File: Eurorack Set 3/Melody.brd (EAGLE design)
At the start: 59.6 x 106.5 mm, 137 parts, among them IC1 LD1117AS33TR, IC3 TL074D, IC4 MCP6004, Q1 MMBT3904, Q2 MMBT3904, Q3 MMBT3904, Q4 MMBT3904, Q5 MMBT3904, Q6 MMBT3904, Q7 MMBT3904, Q8 MMBT3904, U1 MKL02Z32VFK4, U2 LM4040DIM3-5.0, U3 74HC595BQ, U4 74HC595BQ, U5 74HC595BQ, U6 24LC00T-I/OT

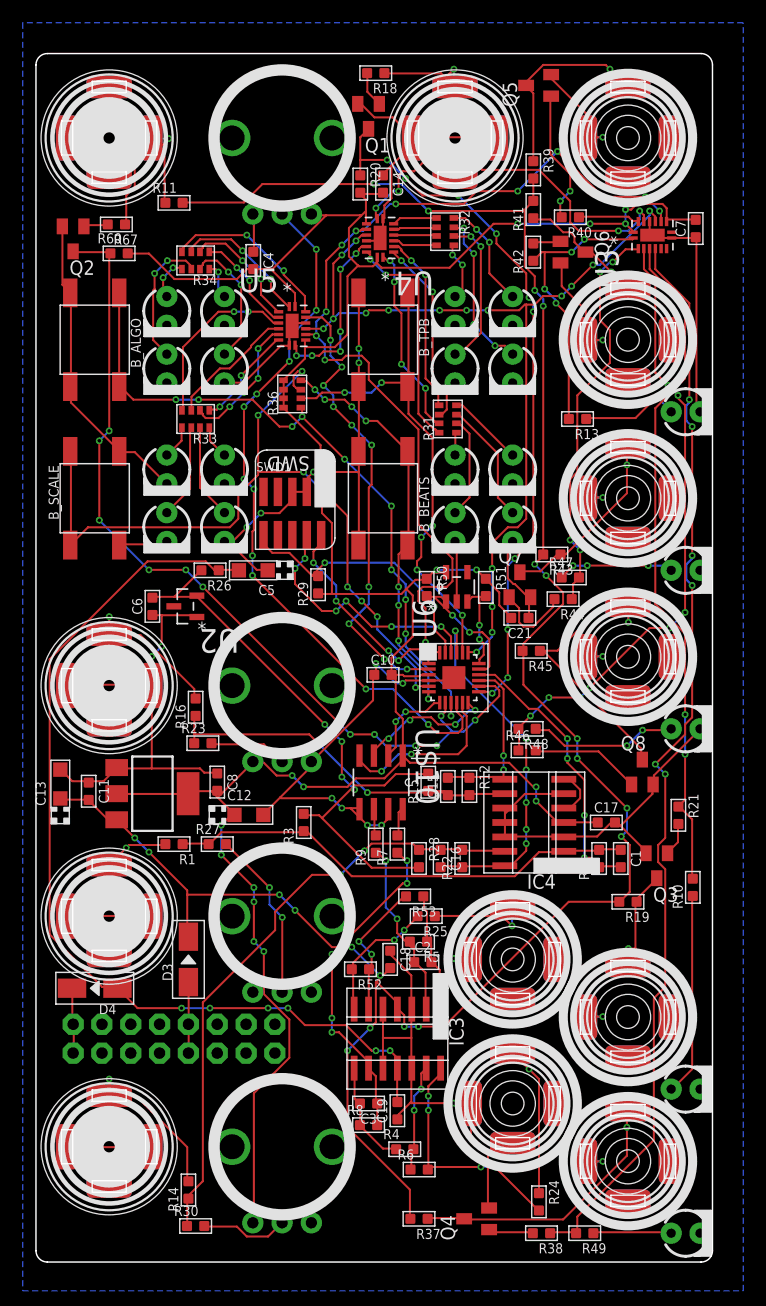
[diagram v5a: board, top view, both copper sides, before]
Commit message: Added Simple Switch Module - Added DESC attribute for some input elements
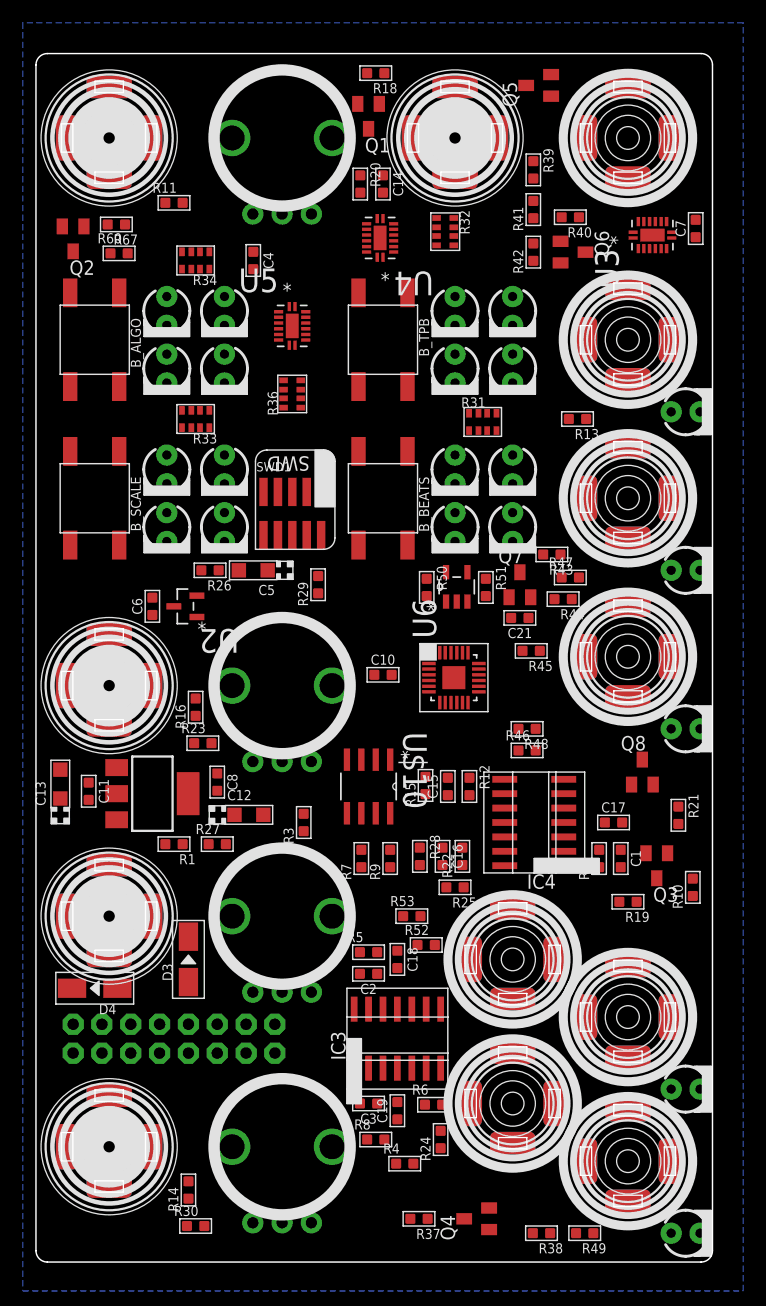
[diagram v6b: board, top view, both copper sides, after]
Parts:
- ACCENT: value ACCENT -> PJ-341
- BEAT: value Beat -> PJ-341
- C1, C15, C16, C2, C3: value 3.3n -> 3.3nF
- CLOCK: value Clock In -> PJ-341
- CLOCKOUT_JACK: value Clock Out -> PJ-341
- GATE: value GATE -> PJ-341
- IN1: value In 1 -> PJ-341
- IN2: value In 2 -> PJ-341
- INTENSITY: value INTENSITY -> PJ-341
- LOOP: value Loop -> PJ-341
- NOTE: value NOTE -> PJ-341
- RESET: value Reset -> PJ-341
- TICK: value Tick -> PJ-341
- VELOCITY: value VELOCITY -> PJ-341
- moved R24 10.3 mm to (36.8, 10.8), turned to 90 degrees
- moved R52 6.18 mm to (35.6, 27.9), turned to 0 degrees
- moved R6 5.85 mm to (36.2, 13.9)
- moved C2 4.89 mm to (30.5, 25.4), turned to 180 degrees
- moved R5 4.50 mm to (30.5, 27.3), turned to 0 degrees
- moved R25 3.59 mm to (38.1, 33.0)
- moved R7 3.42 mm to (29.8, 35.6)
- moved R31 3.09 mm to (40.5, 74.0), turned to 0 degrees
- moved R9 1.80 mm to (32.4, 35.6)
- moved R53 1.76 mm to (34.3, 30.5), turned to 0 degrees
- moved R8 1.42 mm to (31.1, 10.8)
- moved R4 1.27 mm to (33.7, 8.67)
- moved U$10 1.16 mm to (30.5, 41.9)
- moved C18 0.64 mm to (33.0, 26.7)
- moved C17 0.63 mm to (52.1, 38.7)
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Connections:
- removed net N$11: R7.2, U$10.8
- removed net N$12: R9.2, U$10.6
- new net N$5: R9.2, U$10.8
- new net N$7: R7.2, U$10.6
- net N$10: now also IC3.2; no longer IC3.9
- net N$14: now also IC3.7; no longer IC3.14
- net N$17: now also IC3.9; no longer IC3.6
- net N$18: now also IC3.1; no longer IC3.8
- net N$2: now also IC3.6; no longer IC3.13
- net N$24: now also IC3.14; no longer IC3.1
- net N$9: now also IC3.13; no longer IC3.2
- net N$94: now also IC3.8; no longer IC3.7
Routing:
- net GND: track 361.2 -> 0.00 mm, vias 27 -> 0
- net 3.3V: track 246.8 -> 0.00 mm, vias 16 -> 0
- net 12V: track 197.4 -> 0.00 mm, vias 20 -> 0
- net OUT_GATE: track 96.6 -> 0.00 mm, vias 6 -> 0
- net CLOCK: track 84.7 -> 0.00 mm, vias 12 -> 0
- net -12V: track 83.9 -> 0.00 mm, vias 6 -> 0
- net LATCH: track 78.6 -> 0.00 mm, vias 17 -> 0
- net CLOCK_IN: track 78.2 -> 0.00 mm, vias 13 -> 0
- net BUTTON_SCALE: track 70.3 -> 0.00 mm, vias 8 -> 0
- net RESET_PATTERN: track 63.7 -> 0.00 mm, vias 10 -> 0
- net KNOB_TEMPO: track 63.1 -> 0.00 mm, vias 11 -> 0
- net BUTTON_ALGO: track 60.0 -> 0.00 mm, vias 10 -> 0
- net OUT_ACCENT: track 59.8 -> 0.00 mm, vias 2 -> 0
- net OUT_LOOP: track 54.6 -> 0.00 mm, vias 8 -> 0
- net N$34: track 54.0 -> 0.00 mm, vias 2 -> 0
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
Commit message: added router settings, Melody polishing
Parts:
- added U$19: SMALLROCKET, zephod-components:SMALLROCKET
- added U$4, U$7, U$8: FIDUCIAL, adafruit:FIDUCIAL_1MM
- C18, C19: value 100nF -> 100nF 16V+
- moved C7 14.8 mm to (46.3, 84.1)
- moved R42 14.0 mm to (59.0, 88.2)
- moved C18 13.6 mm to (33.0, 13.1), turned to 90 degrees
- moved C19 13.3 mm to (33.2, 26.7), turned to 270 degrees
- moved C14 10.6 mm to (27.0, 85.5), turned to 90 degrees
- moved U3 9.28 mm to (46.2, 89.8), turned to 180 degrees
- moved Q6 6.91 mm to (55.2, 90.5), turned to 90 degrees
- moved R41 6.41 mm to (51.0, 90.5), turned to 180 degrees
- moved R48 5.35 mm to (49.8, 46.2)
- moved R46 5.33 mm to (49.8, 44.5)
- moved R40 5.21 mm to (44.8, 96.0), turned to 90 degrees
- moved R21 4.15 mm to (58.2, 35.2), turned to 180 degrees
- moved Q3 3.78 mm to (56.4, 31.2)
- moved R22 3.51 mm to (42.2, 36.0)
- moved C1 3.32 mm to (56.0, 36.0)
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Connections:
- net GND: now also ACCENT.RING@3, BEAT.RING@3, CLOCK.RING@3, CLOCKOUT_JACK.RING@3, GATE.RING@3, IN1.RING@3, IN1.SWITCH@3, IN2.RING@3, IN2.SWITCH@3, INTENSITY.RING@3, INTENSITY.SWITCH@3, LOOP.RING@3, NOTE.RING@3, RESET.RING@3, RESET.SWITCH@3, TICK.RING@3, VELOCITY.RING@3; no longer ACCENT.RING@1, ACCENT.RING@2, BEAT.RING@1, BEAT.RING@2, CLOCK.RING@1, CLOCK.RING@2, CLOCKOUT_JACK.RING@1, CLOCKOUT_JACK.RING@2, GATE.RING@1, GATE.RING@2, IN1.RING@1, IN1.RING@2, IN1.SWITCH@1, IN1.SWITCH@2, IN2.RING@1, IN2.RING@2, IN2.SWITCH@1, IN2.SWITCH@2, INTENSITY.RING@1, INTENSITY.RING@2, INTENSITY.SWITCH@1, INTENSITY.SWITCH@2, LOOP.RING@1, LOOP.RING@2, NOTE.RING@1, NOTE.RING@2, RESET.RING@1, RESET.RING@2, RESET.SWITCH@1, RESET.SWITCH@2, TICK.RING@1, TICK.RING@2, VELOCITY.RING@1, VELOCITY.RING@2
- net N$16: now also RESET.TIP@3; no longer RESET.TIP@1, RESET.TIP@2
- net N$20: now also VELOCITY.TIP@3; no longer VELOCITY.TIP@1, VELOCITY.TIP@2
- net N$21: now also NOTE.TIP@3; no longer NOTE.TIP@1, NOTE.TIP@2
- net N$29: now also ACCENT.TIP@3; no longer ACCENT.TIP@1, ACCENT.TIP@2
- net N$3: now also IN1.TIP@3; no longer IN1.TIP@1, IN1.TIP@2
- net N$33: now also INTENSITY.TIP@3; no longer INTENSITY.TIP@1, INTENSITY.TIP@2
- net N$43: now also CLOCK.TIP@3; no longer CLOCK.TIP@1, CLOCK.TIP@2
- net N$58: now also GATE.TIP@3; no longer GATE.TIP@1, GATE.TIP@2
- net N$6: now also IN2.TIP@3; no longer IN2.TIP@1, IN2.TIP@2
- net N$61: now also CLOCKOUT_JACK.TIP@3; no longer CLOCKOUT_JACK.TIP@1, CLOCKOUT_JACK.TIP@2
- net N$65: now also TICK.TIP@3; no longer TICK.TIP@1, TICK.TIP@2
- net N$69: now also BEAT.TIP@3; no longer BEAT.TIP@1, BEAT.TIP@2
- net N$72: now also LOOP.TIP@3; no longer LOOP.TIP@1, LOOP.TIP@2
- net N$96: now also CLOCK.SWITCH@3; no longer CLOCK.SWITCH@1, CLOCK.SWITCH@2
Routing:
- net GND: track 0.00 -> 330.8 mm, vias 0 -> 46
- net 3.3V: track 0.00 -> 247.8 mm, vias 0 -> 27
- net 12V: track 0.00 -> 195.6 mm, vias 0 -> 26
- net OUT_GATE: track 0.00 -> 101.2 mm, vias 0 -> 6
- net KNOB_TEMPO: track 0.00 -> 100.7 mm, vias 0 -> 6
- net -12V: track 0.00 -> 87.3 mm, vias 0 -> 4
- net CLOCK_IN: track 0.00 -> 79.9 mm, vias 0 -> 7
- net LATCH: track 0.00 -> 72.0 mm, vias 0 -> 6
- net CLOCK: track 0.00 -> 70.5 mm, vias 0 -> 12
- net BUTTON_SCALE: track 0.00 -> 67.7 mm, vias 0 -> 8
- net OUT_ACCENT: track 0.00 -> 66.5 mm, vias 0 -> 2
- net RESET_PATTERN: track 0.00 -> 63.9 mm, vias 0 -> 10
- net BUTTON_ALGO: track 0.00 -> 63.9 mm, vias 0 -> 4
- net N$34: track 0.00 -> 58.5 mm, vias 0 -> 6
- net REF_-5V: track 0.00 -> 53.3 mm, vias 0 -> 8
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
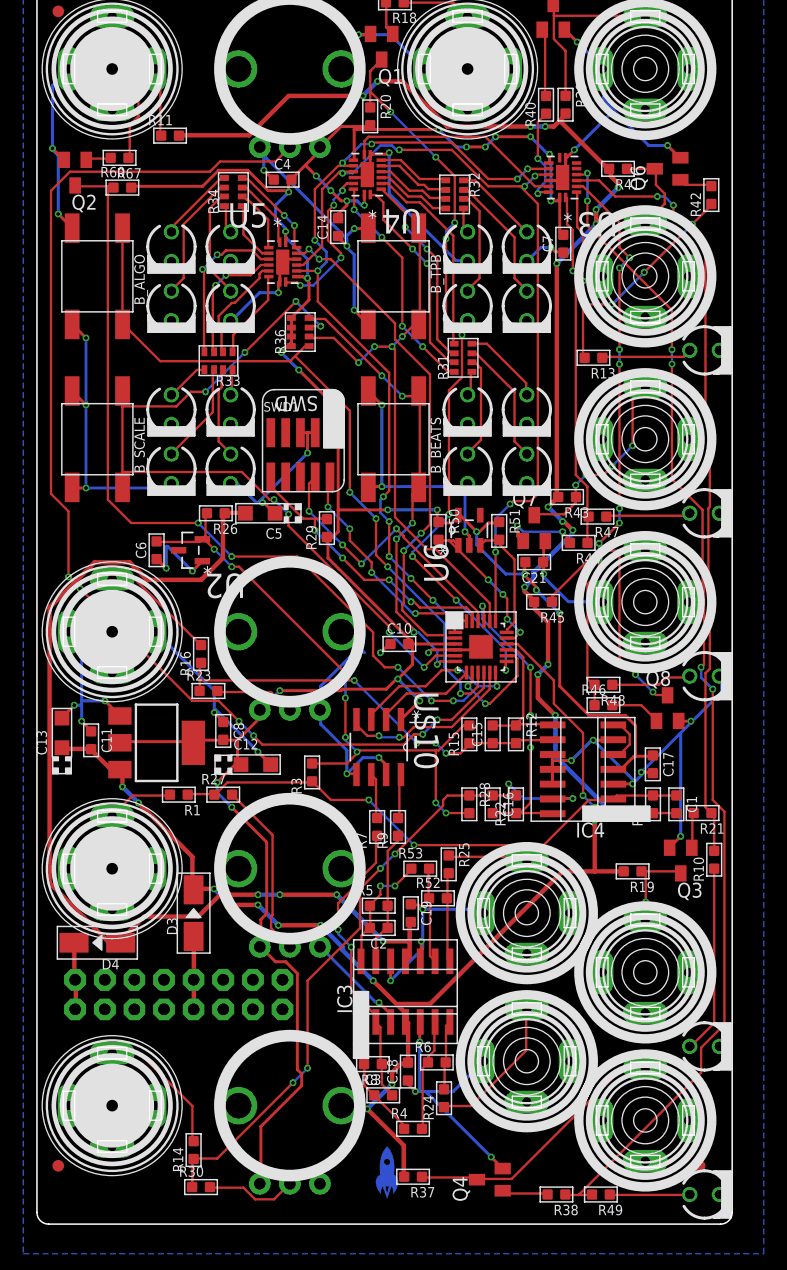
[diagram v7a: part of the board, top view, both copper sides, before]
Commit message: Clearance updates - removed double clocktrace
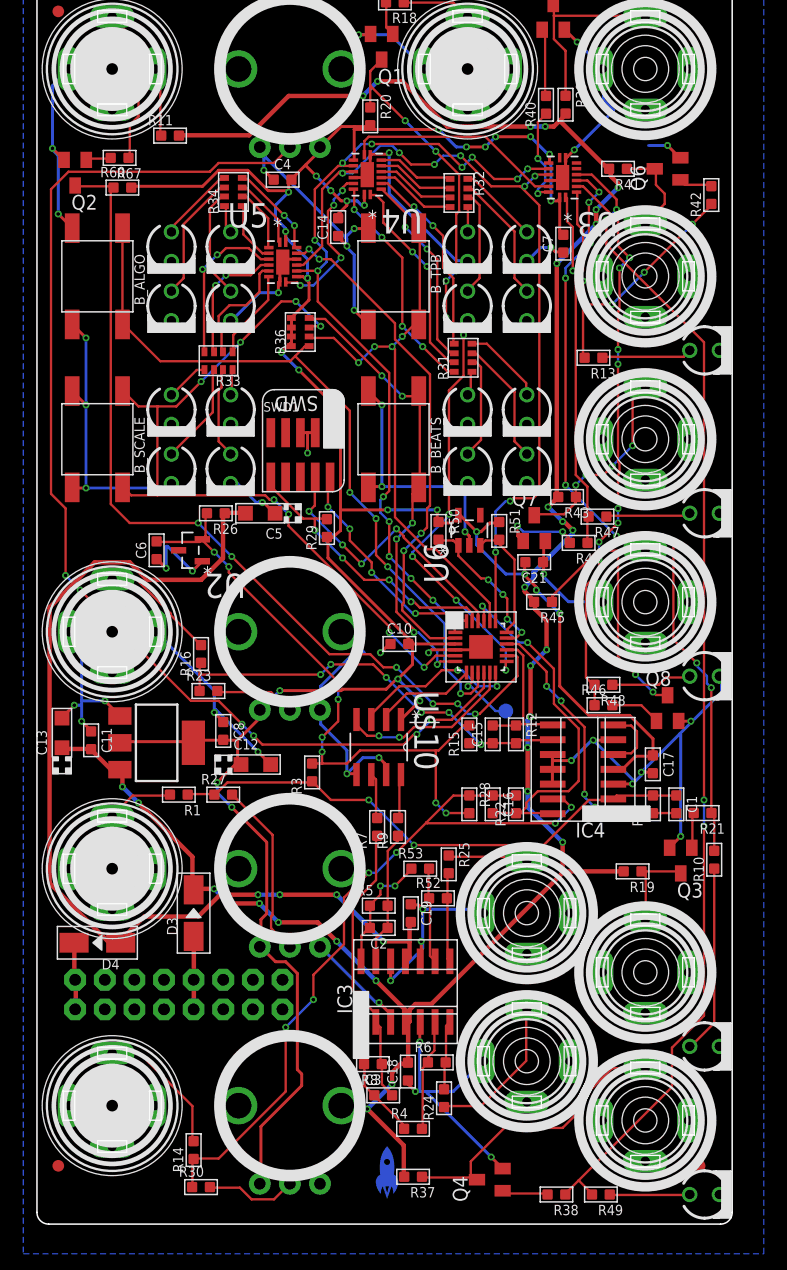
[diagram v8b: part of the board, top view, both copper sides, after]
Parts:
- added TP1: TPB1,27, testpad:B1,27
- moved R32 0.40 mm to (37.4, 88.4)
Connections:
- new net PTA6: TP1.TP, U1.8
- net CLOCK_IN: no longer U1.8
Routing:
- net GND: track 330.8 -> 320.7 mm
- net N$34: track 58.5 -> 64.8 mm
- net PTA6: track 0.00 -> 5.46 mm, vias 0 -> 1
- net ADC_INTENSITY: track 26.4 -> 31.7 mm, vias 4 -> 2
- net CLOCK_IN: track 79.9 -> 77.2 mm, vias 7 -> 6
- net N$58: track 23.2 -> 25.8 mm
- net N$29: track 9.19 -> 7.64 mm, vias 1 -> 0
- net N$97: track 4.42 -> 5.96 mm
- net OUT_ACCENT: track 66.5 -> 68.0 mm, vias 2 -> 8
- net N$4: track 36.0 -> 37.3 mm, vias 4 -> 6
- net OUT_GATE: track 101.2 -> 100.1 mm, vias 6 -> 4
- net LATCH: track 72.0 -> 73.1 mm, vias 6 -> 8
- net N$10: track 25.6 -> 24.6 mm, vias 2 -> 0
- net RESET_PATTERN: track 63.9 -> 64.8 mm
- net 3.3V: track 247.8 -> 248.6 mm
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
